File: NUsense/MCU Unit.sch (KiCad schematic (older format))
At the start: 47 parts

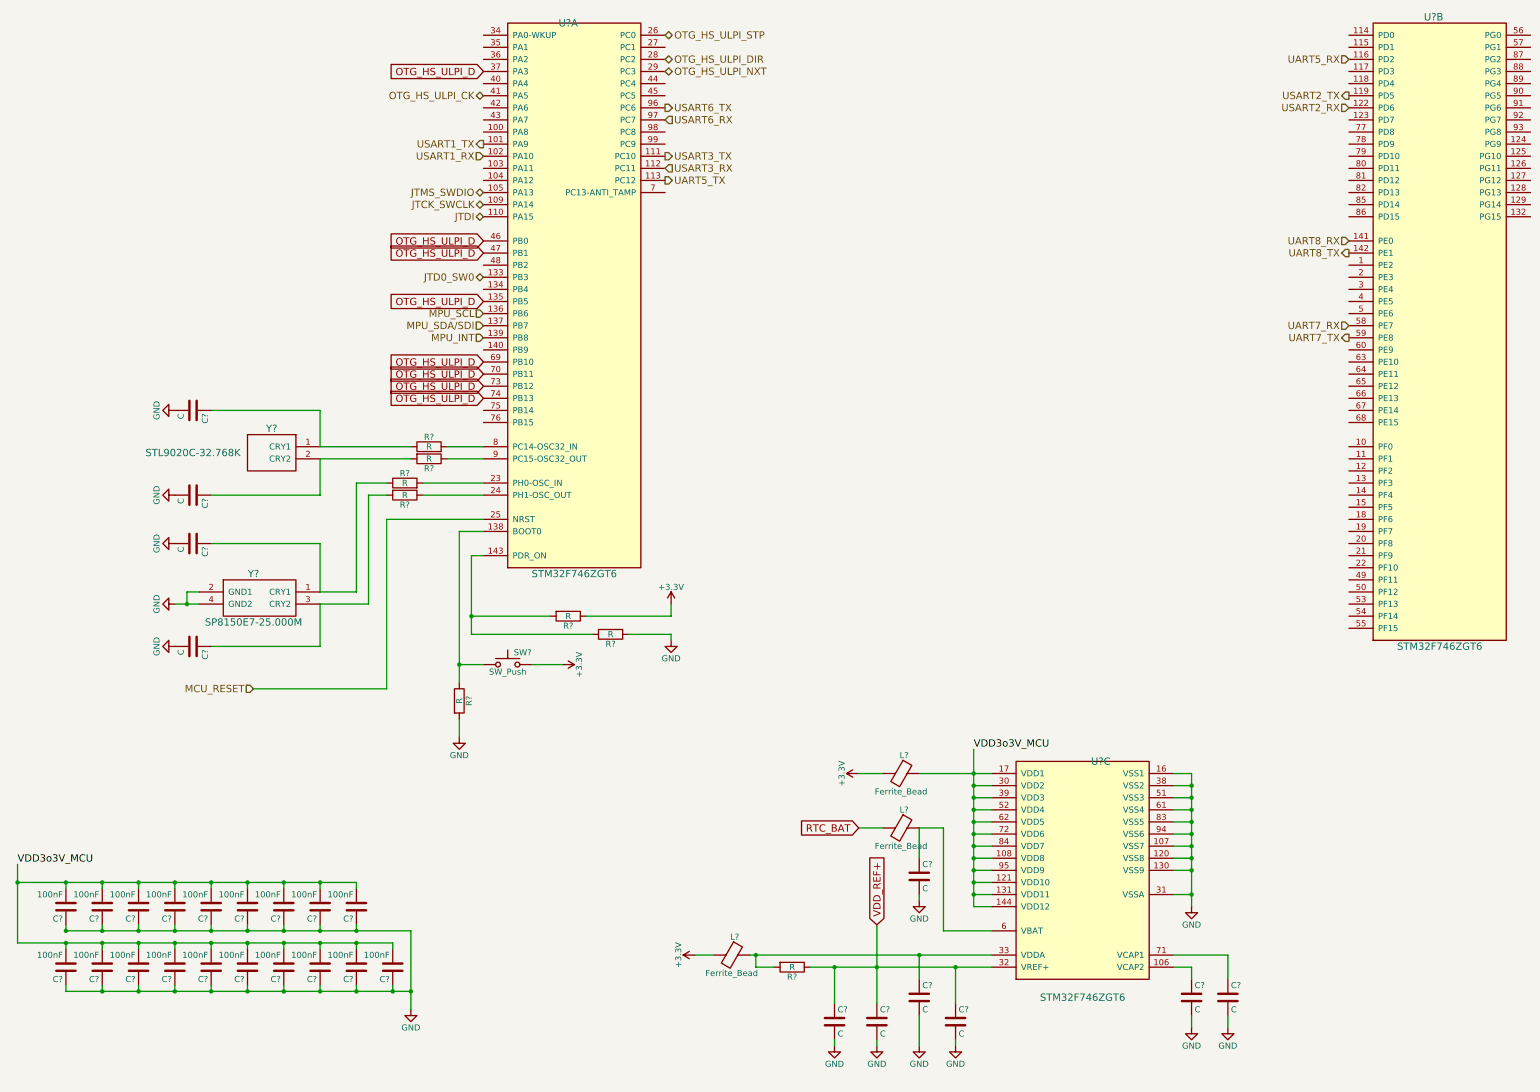
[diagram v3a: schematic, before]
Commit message: Update component values
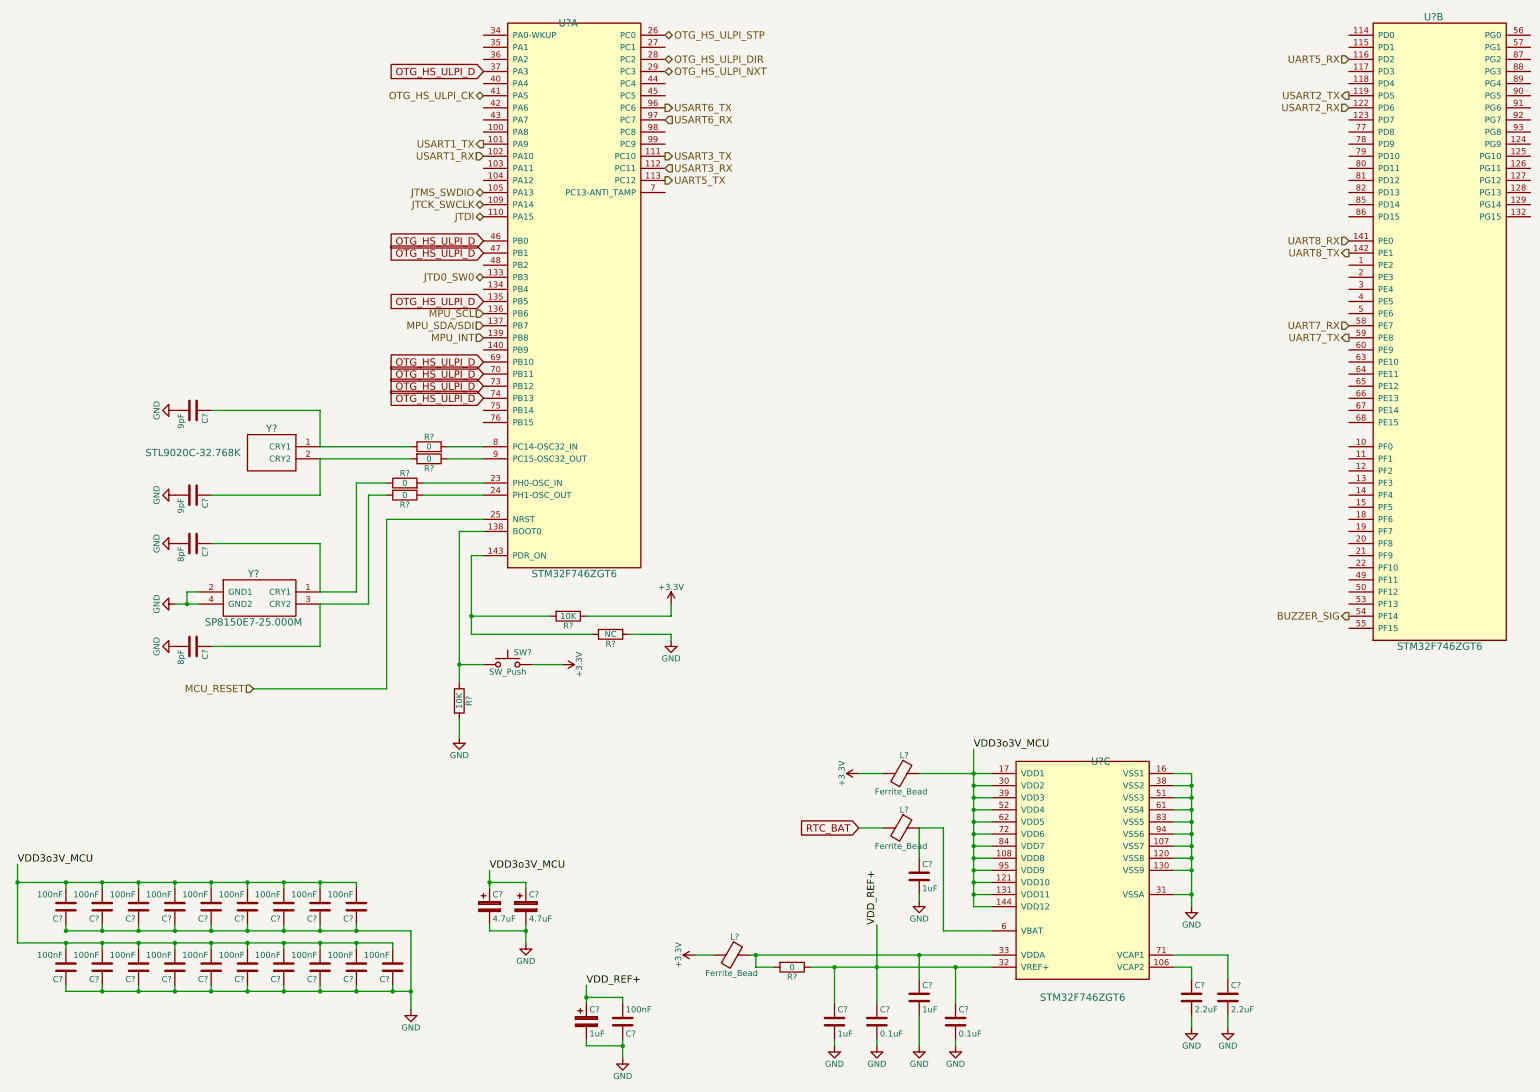
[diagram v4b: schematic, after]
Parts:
- removed C? (x2): C, symbol C
- removed R? (x3): R, symbol R
- added C? (x2): 4.7uF, symbol CP
- added C?: 1uF, symbol CP
- added C?: 100nF, symbol C
- added C?: 9pF, symbol C
- added C?: 8pF, symbol C
- added R? (x3): 0, symbol R
- C?: value C -> 9pF
- C?: value C -> 8pF
- C? (x3): value C -> 1uF
- C? (x2): value C -> 0.1uF
- C? (x2): value C -> 2.2uF
- R? (x2): value R -> 0
- R? (x2): value R -> 10K
- R?: value R -> NC
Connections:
- net GND: now also C?.1, C?.2, C?.2, C?.2, C?.2, C?.2
- net VDD3o3V_MCU: now also C?.1, C?.1
- net VDD_REF+: now also C?.1, C?.2
- net at U?.23 (PH0-OSC_IN): now also R?.2
- net at U?.8 (PC14-OSC32_IN): now also R?.2
- net at U?.9 (PC15-OSC32_OUT): now also R?.1
- net BUZZER_SIG: now reaches U?.54 (PF14)
- net at C?.1, Y?.2 (CRY2): now also R?.2
- net at Y?.1 (CRY1): now also C?.1, R?.1 (x2)
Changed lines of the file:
@@
-$EndComp
-$Comp
-L R R?
-U 1 1 5A6BFE02
-P 4700 5800
-F 0 "R?" V 4780 5800 50  0000 C CNN
-F 1 "R" V 4700 5800 50  0000 C CNN
-F 2 "" V 4630 5800 50  0001 C CNN
-F 3 "" H 4700 5800 50  0001 C CNN
-	1    4700 5800
-	0    1    1    0
-$EndComp
-$Comp
-L R R?
-U 1 1 5A6BFE09
-P 4700 5700
-F 0 "R?" V 4780 5700 50  0000 C CNN
-F 1 "R" V 4700 5700 50  0000 C CNN
-F 2 "" V 4630 5700 50  0001 C CNN
-F 3 "" H 4700 5700 50  0001 C CNN
-	1    4700 5700
-	0    -1   -1   0
 $EndComp
 $Comp
@@
 P 2750 6100
 F 0 "C?" H 2775 6200 50  0000 L CNN
-F 1 "C" H 2775 6000 50  0000 L CNN
+F 1 "9pF" H 2775 6000 50  0000 L CNN
 F 2 "" H 2788 5950 50  0001 C CNN
 F 3 "" H 2750 6100 50  0001 C CNN
 	1    2750 6100
-	0    1    1    0
-$EndComp
-$Comp
-L C C?
-U 1 1 5A6BFE2A
-P 2750 5400
-F 0 "C?" H 2775 5500 50  0000 L CNN
-F 1 "C" H 2775 5300 50  0000 L CNN
-F 2 "" H 2788 5250 50  0001 C CNN
-F 3 "" H 2750 5400 50  0001 C CNN
-	1    2750 5400
 	0    1    1    0
 $EndComp
@@
 $EndComp
 $Comp
-L C C?
-U 1 1 5A6BFE3E
-P 2750 6500
-F 0 "C?" H 2775 6600 50  0000 L CNN
-F 1 "C" H 2775 6400 50  0000 L CNN
-F 2 "" H 2788 6350 50  0001 C CNN
-F 3 "" H 2750 6500 50  0001 C CNN
-	1    2750 6500
-	0    1    1    0
-$EndComp
-$Comp
 L GND #PWR?
 U 1 1 5A6BFE45
@@
 P 2750 7350
 F 0 "C?" H 2775 7450 50  0000 L CNN
-F 1 "C" H 2775 7250 50  0000 L CNN
+F 1 "8pF" H 2775 7250 50  0000 L CNN
 F 2 "" H 2788 7200 50  0001 C CNN
 F 3 "" H 2750 7350 50  0001 C CNN
@@
 P 4500 6100
 F 0 "R?" V 4580 6100 50  0000 C CNN
-F 1 "R" V 4500 6100 50  0000 C CNN
+F 1 "0" V 4500 6100 50  0000 C CNN
 F 2 "" V 4430 6100 50  0001 C CNN
 F 3 "" H 4500 6100 50  0001 C CNN
 	1    4500 6100
 	0    1    1    0
-$EndComp
-$Comp
-L R R?
-U 1 1 5A6BFE5F
-P 4500 6000
-F 0 "R?" V 4580 6000 50  0000 C CNN
-F 1 "R" V 4500 6000 50  0000 C CNN
-F 2 "" V 4430 6000 50  0001 C CNN
-F 3 "" H 4500 6000 50  0001 C CNN
-	1    4500 6000
-	0    -1   -1   0
 $EndComp
 $Comp
@@
 P 5850 7100
 F 0 "R?" V 5930 7100 50  0000 C CNN
-F 1 "R" V 5850 7100 50  0000 C CNN
+F 1 "10K" V 5850 7100 50  0000 C CNN
 F 2 "" V 5780 7100 50  0001 C CNN
 F 3 "" H 5850 7100 50  0001 C CNN
@@
 P 6200 7250
 F 0 "R?" V 6280 7250 50  0000 C CNN
-F 1 "R" V 6200 7250 50  0000 C CNN
+F 1 "NC" V 6200 7250 50  0000 C CNN
 F 2 "" V 6130 7250 50  0001 C CNN
 F 3 "" H 6200 7250 50  0001 C CNN
@@
 P 4950 7800
 F 0 "R?" V 5030 7800 50  0000 C CNN
-F 1 "R" V 4950 7800 50  0000 C CNN
+F 1 "10K" V 4950 7800 50  0000 C CNN
 F 2 "" V 4880 7800 50  0001 C CNN
 F 3 "" H 4950 7800 50  0001 C CNN
@@
 P 8750 9250
 F 0 "C?" H 8775 9350 50  0000 L CNN
-F 1 "C" H 8775 9150 50  0000 L CNN
+F 1 "1uF" H 8775 9150 50  0000 L CNN
 F 2 "" H 8788 9100 50  0001 C CNN
 F 3 "" H 8750 9250 50  0001 C CNN
@@
 P 9050 10450
 F 0 "C?" H 9075 10550 50  0000 L CNN
-F 1 "C" H 9075 10350 50  0000 L CNN
+F 1 "0.1uF" H 9075 10350 50  0000 L CNN
 F 2 "" H 9088 10300 50  0001 C CNN
 F 3 "" H 9050 10450 50  0001 C CNN
@@
 P 8750 10250
 F 0 "C?" H 8775 10350 50  0000 L CNN
-F 1 "C" H 8775 10150 50  0000 L CNN
+F 1 "1uF" H 8775 10150 50  0000 L CNN
 F 2 "" H 8788 10100 50  0001 C CNN
 F 3 "" H 8750 10250 50  0001 C CNN
@@
 P 8400 10450
 F 0 "C?" H 8425 10550 50  0000 L CNN
-F 1 "C" H 8425 10350 50  0000 L CNN
+F 1 "0.1uF" H 8425 10350 50  0000 L CNN
 F 2 "" H 8438 10300 50  0001 C CNN
 F 3 "" H 8400 10450 50  0001 C CNN
@@
 P 8050 10450
 F 0 "C?" H 8075 10550 50  0000 L CNN
-F 1 "C" H 8075 10350 50  0000 L CNN
+F 1 "1uF" H 8075 10350 50  0000 L CNN
 F 2 "" H 8088 10300 50  0001 C CNN
 F 3 "" H 8050 10450 50  0001 C CNN
@@
 P 7700 10000
 F 0 "R?" V 7780 10000 50  0000 C CNN
-F 1 "R" V 7700 10000 50  0000 C CNN
+F 1 "0" V 7700 10000 50  0000 C CNN
 F 2 "" V 7630 10000 50  0001 C CNN
 F 3 "" H 7700 10000 50  0001 C CNN
@@
 	1    0    0    -1
 $EndComp
-Text GLabel 8400 9650 1    60   Input ~ 0
-VDD_REF+
 $Comp
 L GND #PWR?
@@
 P 11000 10250
 F 0 "C?" H 11025 10350 50  0000 L CNN
-F 1 "C" H 11025 10150 50  0000 L CNN
+F 1 "2.2uF" H 11025 10150 50  0000 L CNN
 F 2 "" H 11038 10100 50  0001 C CNN
 F 3 "" H 11000 10250 50  0001 C CNN
@@
 P 11300 10250
 F 0 "C?" H 11325 10350 50  0000 L CNN
-F 1 "C" H 11325 10150 50  0000 L CNN
+F 1 "2.2uF" H 11325 10150 50  0000 L CNN
 F 2 "" H 11338 10100 50  0001 C CNN
 F 3 "" H 11300 10250 50  0001 C CNN
@@
 	8050 10300 8050 10000
 Connection ~ 8050 10000
-Wire Wire Line
-	8400 9650 8400 10300
 Connection ~ 8400 10000
 Wire Wire Line
@@
 	1    5800 7500
 	0    1    1    0
-$EndComp
-$Comp
-L +3.3V #PWR?
-U 1 1 5A6FD08D
-P 6900 9900
-F 0 "#PWR?" H 6900 9750 50  0001 C CNN
-F 1 "+3.3V" H 6900 10040 50  0000 C CNN
-F 2 "" H 6900 9900 50  0001 C CNN
-F 3 "" H 6900 9900 50  0001 C CNN
-	1    6900 9900
-	0    -1   -1   0
 $EndComp
 $Comp
@@
 Connection ~ 2000 10200
 Connection ~ 4550 10200
+$Comp
+L CP C?
+U 1 1 5A700B8B
+P 5200 9500
+F 0 "C?" H 5225 9600 50  0000 L CNN
+F 1 "4.7uF" H 5225 9400 50  0000 L CNN
+F 2 "" H 5238 9350 50  0001 C CNN
+F 3 "" H 5200 9500 50  0001 C CNN
+	1    5200 9500
+	1    0    0    -1
+$EndComp
+$Comp
+L CP C?
+U 1 1 5A700CDA
+P 5500 9500
+F 0 "C?" H 5525 9600 50  0000 L CNN
+F 1 "4.7uF" H 5525 9400 50  0000 L CNN
+F 2 "" H 5538 9350 50  0001 C CNN
+F 3 "" H 5500 9500 50  0001 C CNN
+	1    5500 9500
+	1    0    0    -1
+$EndComp
+Wire Wire Line
+	5200 9200 5200 9350
+Wire Wire Line
+	5200 9300 5500 9300
+Wire Wire Line
+	5500 9300 5500 9350
+Wire Wire Line
+	5500 9650 5500 9800
+Wire Wire Line
+	5500 9700 5200 9700
+Wire Wire Line
+	5200 9700 5200 9650
+Connection ~ 5500 9700
+Connection ~ 5200 9300
+Text Label 5200 9200 0    60   ~ 0
+VDD3o3V_MCU
+$Comp
+L GND #PWR?
+U 1 1 5A701246
+P 5500 9800
+F 0 "#PWR?" H 5500 9550 50  0001 C CNN
+F 1 "GND" H 5500 9650 50  0000 C CNN
+F 2 "" H 5500 9800 50  0001 C CNN
+F 3 "" H 5500 9800 50  0001 C CNN
+	1    5500 9800
+	1    0    0    -1
+$EndComp
+Wire Wire Line
+	6000 10150 6000 10300
+Wire Wire Line
+	6000 10250 6300 10250
+Wire Wire Line
+	6300 10250 6300 10300
+Wire Wire Line
+	6300 10600 6300 10750
+Wire Wire Line
+	6300 10650 6000 10650
+Wire Wire Line
+	6000 10650 6000 10600
+Connection ~ 6300 10650
+Connection ~ 6000 10250
+Text Label 6000 10150 0    60   ~ 0
+VDD_REF+
+$Comp
+L GND #PWR?
+U 1 1 5A7014A6
+P 6300 10750
+F 0 "#PWR?" H 6300 10500 50  0001 C CNN
+F 1 "GND" H 6300 10600 50  0000 C CNN
+F 2 "" H 6300 10750 50  0001 C CNN
+F 3 "" H 6300 10750 50  0001 C CNN
+	1    6300 10750
+	1    0    0    -1
+$EndComp
+Text Label 8400 9650 1    60   ~ 0
+VDD_REF+
+$Comp
+L CP C?
+U 1 1 5A7018A5
+P 6000 10450
+F 0 "C?" H 6025 10550 50  0000 L CNN
+F 1 "1uF" H 6025 10350 50  0000 L CNN
+F 2 "" H 6038 10300 50  0001 C CNN
+F 3 "" H 6000 10450 50  0001 C CNN
+	1    6000 10450
+	1    0    0    -1
+$EndComp
+$Comp
+L C C?
+U 1 1 5A701A0C
+P 6300 10450
+F 0 "C?" H 6325 10550 50  0000 L CNN
+F 1 "100nF" H 6325 10350 50  0000 L CNN
+F 2 "" H 6338 10300 50  0001 C CNN
+F 3 "" H 6300 10450 50  0001 C CNN
+	1    6300 10450
+	1    0    0    1
+$EndComp
+Wire Wire Line
+	8400 9650 8400 10300
+$Comp
+L +3.3V #PWR?
+U 1 1 5A6FD08D
+P 6900 9900
+F 0 "#PWR?" H 6900 9750 50  0001 C CNN
+F 1 "+3.3V" H 6900 10040 50  0000 C CNN
+F 2 "" H 6900 9900 50  0001 C CNN
+F 3 "" H 6900 9900 50  0001 C CNN
+	1    6900 9900
+	0    -1   -1   0
+$EndComp
+$Comp
+L C C?
+U 1 1 5A703D4E
+P 2750 5400
+F 0 "C?" H 2775 5500 50  0000 L CNN
+F 1 "9pF" H 2775 5300 50  0000 L CNN
+F 2 "" H 2788 5250 50  0001 C CNN
+F 3 "" H 2750 5400 50  0001 C CNN
+	1    2750 5400
+	0    1    1    0
+$EndComp
+$Comp
+L C C?
+U 1 1 5A703E06
+P 2750 6500
+F 0 "C?" H 2775 6600 50  0000 L CNN
+F 1 "8pF" H 2775 6400 50  0000 L CNN
+F 2 "" H 2788 6350 50  0001 C CNN
+F 3 "" H 2750 6500 50  0001 C CNN
+	1    2750 6500
+	0    1    1    0
+$EndComp
+$Comp
+L R R?
+U 1 1 5A7040F6
+P 4700 5800
+F 0 "R?" V 4780 5800 50  0000 C CNN
+F 1 "0" V 4700 5800 50  0000 C CNN
+F 2 "" V 4630 5800 50  0001 C CNN
+F 3 "" H 4700 5800 50  0001 C CNN
+	1    4700 5800
+	0    1    1    0
+$EndComp
+$Comp
+L R R?
+U 1 1 5A7041AB
+P 4700 5700
+F 0 "R?" V 4780 5700 50  0000 C CNN
+F 1 "0" V 4700 5700 50  0000 C CNN
+F 2 "" V 4630 5700 50  0001 C CNN
+F 3 "" H 4700 5700 50  0001 C CNN
+	1    4700 5700
+	0    -1   -1   0
+$EndComp
+$Comp
+L R R?
+U 1 1 5A70425B
+P 4500 6000
+F 0 "R?" V 4580 6000 50  0000 C CNN
+F 1 "0" V 4500 6000 50  0000 C CNN
+F 2 "" V 4430 6000 50  0001 C CNN
+F 3 "" H 4500 6000 50  0001 C CNN
+	1    4500 6000
+	0    -1   -1   0
+$EndComp
+Text HLabel 12300 7100 0    60   Output ~ 0
+BUZZER_SIG
 $EndSCHEMATC
